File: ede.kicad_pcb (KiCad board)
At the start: 4 copper layers, 72.1 x 49 mm, 114 parts, among them J1 Conn_01x01, J10 Conn_01x01, J11 Conn_01x01, J12 Conn_01x01, J2 Conn_01x01, J3 Conn_01x01, J4 Conn_01x01, J5 Conn_01x06, J6 Conn_01x01, J7 Conn_01x04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

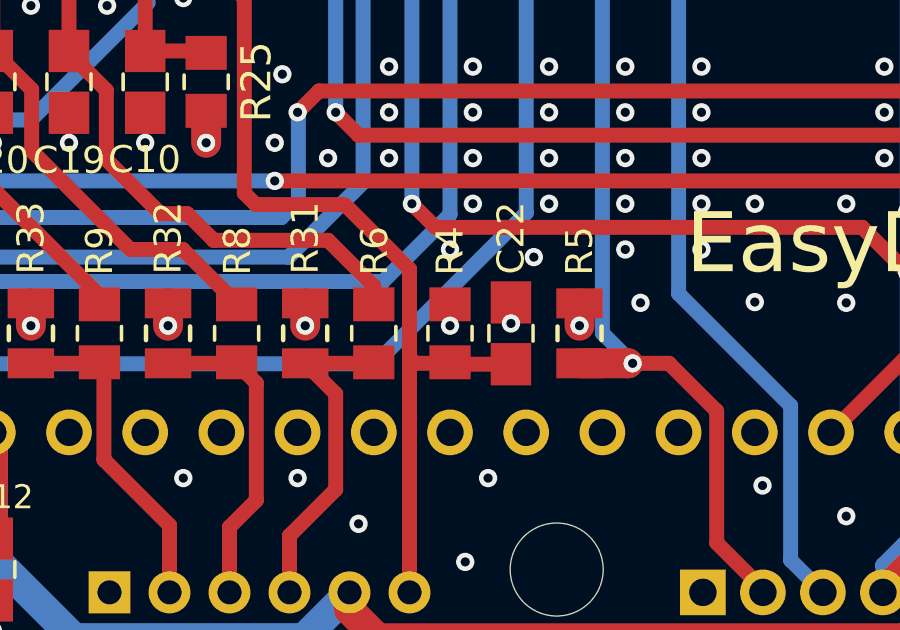
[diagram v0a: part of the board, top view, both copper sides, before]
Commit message: pcb: T.Cu Mtr temp resistor 3.3V via to track improvement
Signed-off-by: Afzal <afzal@intible.in>
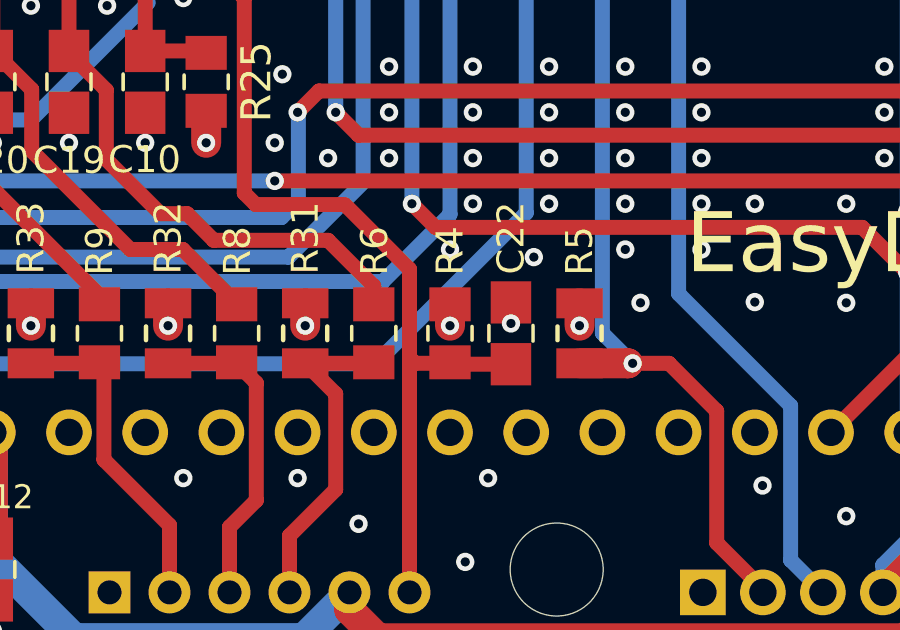
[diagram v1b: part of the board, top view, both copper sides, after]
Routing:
- net +3V3: track 143.3 -> 144.1 mm
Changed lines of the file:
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@@
   (segment (start 48.0728 107.2876) (end 50.1028 105.2576) (width 0.5) (layer "F.Cu") (net 37))
   (segment (start 52.9078 105.5116) (end 50.3568 105.5116) (width 1) (layer "F.Cu") (net 37))
+  (segment (start 86.9188 105.5611) (end 86.9188 106.2736) (width 1) (layer "F.Cu") (net 37))
   (segment (start 110.0188 94.8296) (end 109.7788 94.5896) (width 1) (layer "F.Cu") (net 37))
   (segment (start 66.5988 106.3976) (end 66.5988 109.8296) (width 1) (layer "F.Cu") (net 37))
